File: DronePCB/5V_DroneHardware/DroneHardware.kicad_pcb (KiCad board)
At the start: 4 copper layers, 36.1 x 36 mm, 50 parts, among them J201 USB_B_Micro, J202 BATTERY, J203 SWD_CONN, J204 Conn_01x06_Male, J205 Conn_01x03_Female, J206 Conn_01x03_Female, J207 Conn_01x03_Female, J208 Conn_01x03_Female, J209 Conn_01x03_Female, J210 Conn_01x03_Female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

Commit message: Aggiunta dell'alimentazine della radio e il GND
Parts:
- added J101: +5V, Connector_PinHeader_1.00mm:PinHeader_1x01_P1.00mm_Vertical, F.Cu at (151.6, 111.4)
- added J102: GND, Connector_PinHeader_1.00mm:PinHeader_1x04_P1.00mm_Vertical, F.Cu at (135.7, 117.4)
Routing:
- net BUCK_IN: track 5.21 -> 12.9 mm
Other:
- board text added: "R_5V"
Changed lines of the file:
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@@
+    )
+  )
+  (footprint "Connector_PinHeader_1.00mm:PinHeader_1x01_P1.00mm_Vertical" (layer "F.Cu")
+    (at 151.55 111.44)
+    (descr "Through hole straight pin header, 1x01, 1.00mm pitch, single row")
+    (tags "Through hole pin header THT 1x01 1.00mm single row")
+    (property "Sheetfile" "Power.kicad_sch")
+    (property "Sheetname" "Power, Start: 100")
+    (attr through_hole)
+    (fp_text reference "J101" (at 0 -1.56) (layer "F.Fab")
+      (effects (font (size 1 1) (thickness 0.15)))
+    )
+    (fp_text value "+5V" (at 0 1.56) (layer "F.Fab")
+      (effects (font (size 1 1) (thickness 0.15)))
+    )
+    (fp_text user "${REFERENCE}" (at 0 0 90) (layer "F.Fab")
+      (effects (font (size 0.76 0.76) (thickness 0.114)))
+    )
+    (fp_line (start -0.695 0) (end -0.695 -0.685) (layer "F.SilkS") (width 0.12))
+    (fp_line (start 0.695 0.685) (end 0.695 0.56) (layer "F.SilkS") (width 0.12))
+    (fp_line (start -0.695 0.685) (end -0.695 0.56) (layer "F.SilkS") (width 0.12))
+    (fp_line (start -0.695 -0.685) (end 0 -0.685) (layer "F.SilkS") (width 0.12))
+    (fp_line (start 0.608276 0.685) (end 0.695 0.685) (layer "F.SilkS") (width 0.12))
+    (fp_line (start -0.695 0.685) (end -0.608276 0.685) (layer "F.SilkS") (width 0.12))
+    (fp_line (start -0.695 0.685) (end 0.695 0.685) (layer "F.SilkS") (width 0.12))
+    (fp_line (start 1.15 -1) (end -1.15 -1) (layer "F.CrtYd") (width 0.05))
+    (fp_line (start -1.15 1) (end 1.15 1) (layer "F.CrtYd") (width 0.05))
+    (fp_line (start 1.15 1) (end 1.15 -1) (layer "F.CrtYd") (width 0.05))
+    (fp_line (start -1.15 -1) (end -1.15 1) (layer "F.CrtYd") (width 0.05))
+    (fp_line (start -0.635 -0.1825) (end -0.3175 -0.5) (layer "F.Fab") (width 0.1))
+    (fp_line (start 0.635 0.5) (end -0.635 0.5) (layer "F.Fab") (width 0.1))
+    (fp_line (start 0.635 -0.5) (end 0.635 0.5) (layer "F.Fab") (width 0.1))
+    (fp_line (start -0.635 0.5) (end -0.635 -0.1825) (layer "F.Fab") (width 0.1))
+    (fp_line (start -0.3175 -0.5) (end 0.635 -0.5) (layer "F.Fab") (width 0.1))
+    (pad "1" thru_hole rect (at 0 0) (size 0.85 0.85) (drill 0.5) (layers *.Cu *.Mask)
+      (net 5 "BUCK_IN") (pinfunction "Pin_1") (pintype "passive"))
+    (model "${KICAD6_3DMODEL_DIR}/Connector_PinHeader_1.00mm.3dshapes/PinHeader_1x01_P1.00mm_Vertical.wrl"
+      (offset (xyz 0 0 0))
+      (scale (xyz 1 1 1))
+      (rotate (xyz 0 0 0))
     )
   )
@@
     )
   )
+  (footprint "Connector_PinHeader_1.00mm:PinHeader_1x04_P1.00mm_Vertical" (layer "F.Cu")
+    (at 135.71 117.41 90)
+    (descr "Through hole straight pin header, 1x04, 1.00mm pitch, single row")
+    (tags "Through hole pin header THT 1x04 1.00mm single row")
+    (property "Sheetfile" "Power.kicad_sch")
+    (property "Sheetname" "Power, Start: 100")
+    (attr through_hole)
+    (fp_text reference "J102" (at 0 -1.56 90) (layer "F.Fab")
+      (effects (font (size 1 1) (thickness 0.15)))
+    )
+    (fp_text value "GND" (at 0 4.56 90) (layer "F.Fab")
+      (effects (font (size 1 1) (thickness 0.15)))
+    )
+    (fp_text user "${REFERENCE}" (at 0 1.5) (layer "F.Fab")
+      (effects (font (size 0.76 0.76) (thickness 0.114)))
+    )
+    (fp_line (start 0.608276 0.685) (end 0.695 0.685) (layer "F.SilkS") (width 0.12))
+    (fp_line (start -0.695 0) (end -0.695 -0.685) (layer "F.SilkS") (width 0.12))
+    (fp_line (start -0.695 3.56) (end -0.394493 3.56) (layer "F.SilkS") (width 0.12))
+    (fp_line (start -0.695 0.685) (end -0.608276 0.685) (layer "F.SilkS") (width 0.12))
+    (fp_line (start -0.695 -0.685) (end 0 -0.685) (layer "F.SilkS") (width 0.12))
+    (fp_line (start 0.394493 3.56) (end 0.695 3.56) (layer "F.SilkS") (width 0.12))
+    (fp_line (start 0.695 0.685) (end 0.695 3.56) (layer "F.SilkS") (width 0.12))
+    (fp_line (start -0.695 0.685) (end -0.695 3.56) (layer "F.SilkS") (width 0.12))
+    (fp_line (start -1.15 4) (end 1.15 4) (layer "F.CrtYd") (width 0.05))
+    (fp_line (start 1.15 4) (end 1.15 -1) (layer "F.CrtYd") (width 0.05))
+    (fp_line (start -1.15 -1) (end -1.15 4) (layer "F.CrtYd") (width 0.05))
+    (fp_line (start 1.15 -1) (end -1.15 -1) (layer "F.CrtYd") (width 0.05))
+    (fp_line (start -0.635 -0.1825) (end -0.3175 -0.5) (layer "F.Fab") (width 0.1))
+    (fp_line (start -0.3175 -0.5) (end 0.635 -0.5) (layer "F.Fab") (width 0.1))
+    (fp_line (start 0.635 -0.5) (end 0.635 3.5) (layer "F.Fab") (width 0.1))
+    (fp_line (start 0.635 3.5) (end -0.635 3.5) (layer "F.Fab") (width 0.1))
+    (fp_line (start -0.635 3.5) (end -0.635 -0.1825) (layer "F.Fab") (width 0.1))
+    (pad "1" thru_hole rect (at 0 0 90) (size 0.85 0.85) (drill 0.5) (layers *.Cu *.Mask)
+      (net 2 "GND") (pinfunction "Pin_1") (pintype "passive"))
+    (pad "2" thru_hole oval (at 0 1 90) (size 0.85 0.85) (drill 0.5) (layers *.Cu *.Mask)
+      (net 2 "GND") (pinfunction "Pin_2") (pintype "passive"))
+    (pad "3" thru_hole oval (at 0 2 90) (size 0.85 0.85) (drill 0.5) (layers *.Cu *.Mask)
+      (net 2 "GND") (pinfunction "Pin_3") (pintype "passive"))
+    (pad "4" thru_hole oval (at 0 3 90) (size 0.85 0.85) (drill 0.5) (layers *.Cu *.Mask)
+      (net 2 "GND") (pinfunction "Pin_4") (pintype "passive"))
+    (model "${KICAD6_3DMODEL_DIR}/Connector_PinHeader_1.00mm.3dshapes/PinHeader_1x04_P1.00mm_Vertical.wrl"
+      (offset (xyz 0 0 0))
+      (scale (xyz 1 1 1))
+      (rotate (xyz 0 0 0))
+    )
+  )
   (footprint "Resistor_SMD:R_0603_1608Metric" (layer "F.Cu")
     (at 160.07 110.84 -90)
@@
     (at 156.23 106.85 180)
     (attr board_only exclude_from_pos_files exclude_from_bom)
-    (fp_text reference "G***" (at 0 0) (layer "B.Fab")
+    (fp_text reference "G***" (at 0 0) (layer "F.Fab")
       (effects (font (size 1.524 1.524) (thickness 0.3)) (justify mirror))
     )
-    (fp_text value "LOGO" (at 0.75 0) (layer "B.Fab") hide
+    (fp_text value "LOGO" (at 0.75 0) (layer "F.Fab") hide
       (effects (font (size 1.524 1.524) (thickness 0.3)) (justify mirror))
     )
@@
       ) (layer "B.SilkS") (width 0) (fill solid))
   )
+  (gr_line (start 134.79 118.8) (end 141.37 118.79) (layer "F.SilkS") (width 0.15))
   (gr_arc (start 130.548478 119.07) (mid 128.710272 118.299778) (end 127.940001 116.461592) (layer "Edge.Cuts") (width 0.1))
   (gr_arc (start 161.441522 83.078478) (mid 163.286553 83.839188) (end 164.061432 85.678313) (layer "Edge.Cuts") (width 0.1))
@@
     (effects (font (size 0.5 0.5) (thickness 0.1)))
   )
+  (gr_text "R_5V\n" (at 151.42 112.85) (layer "F.SilkS")
+    (effects (font (size 0.5 0.5) (thickness 0.1)))
+  )
   (gr_text "GND\n" (at 150.87 117.85) (layer "F.SilkS")
     (effects (font (size 0.5 0.5) (thickness 0.1)))
@@
   )
   (gr_text "4" (at 132.28 103.54) (layer "F.SilkS")
+    (effects (font (size 0.5 0.5) (thickness 0.1)))
+  )
+  (gr_text "GND\n" (at 140.74 118.25) (layer "F.SilkS")
     (effects (font (size 0.5 0.5) (thickness 0.1)))
   )
@@
   (segment (start 137.16 97.14) (end 137.85 97.83) (width 0.3) (layer "F.Cu") (net 4))
   (segment (start 158.275 110.48) (end 158.275 112.5525) (width 0.6) (layer "F.Cu") (net 5))
+  (segment (start 157.66 107.72) (end 155.27 107.72) (width 0.6) (layer "F.Cu") (net 5))
   (segment (start 158.275 112.5525) (end 158.3625 112.64) (width 0.6) (layer "F.Cu") (net 5))
+  (segment (start 155.27 107.72) (end 151.55 111.44) (width 0.6) (layer "F.Cu") (net 5))
   (segment (start 157.66 109.865) (end 158.275 110.48) (width 0.6) (layer "F.Cu") (net 5))
   (segment (start 157.66 107.72) (end 157.66 109.865) (width 0.6) (layer "F.Cu") (net 5))

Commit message: BOM e pos file
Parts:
- C102: footprint Capacitor_SMD:C_0201_0603Metric -> Capacitor_Tantalum_SMD:CP_EIA-1608-08_AVX-J
- moved R101 0.63 mm to (160.0, 111.5)
- moved D102 0.52 mm to (162.4, 112.1)
- moved C102 0.50 mm to (162.4, 110.0)
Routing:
- net GND: track 41.8 -> 43.7 mm, vias 31 -> 30
- net BUCK_VOUT_3V3: track 27.0 -> 28.2 mm

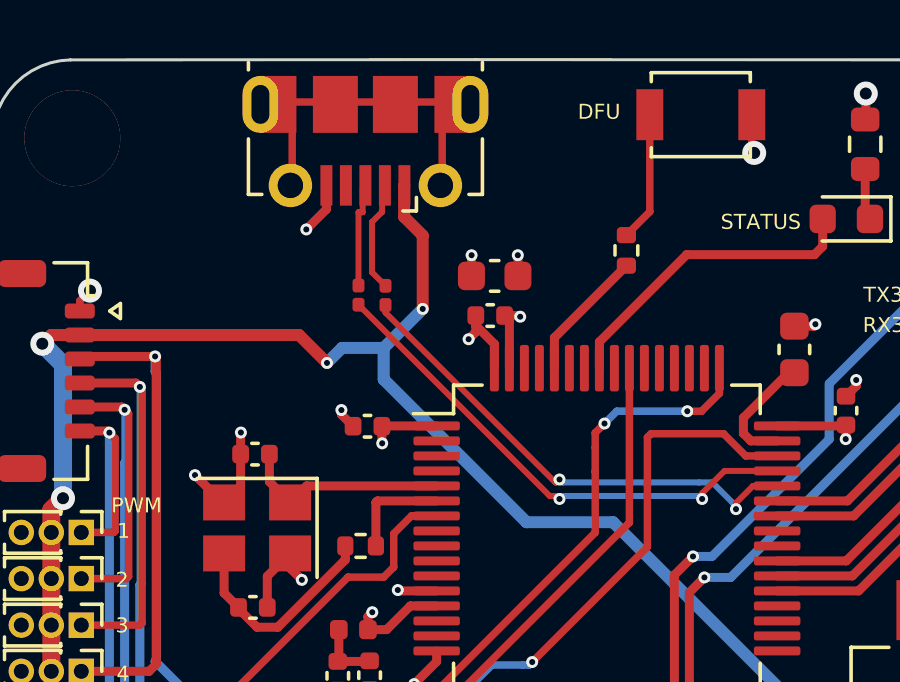
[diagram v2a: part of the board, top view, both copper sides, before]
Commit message: Modifica delle componenti 0201 in componenti 0402
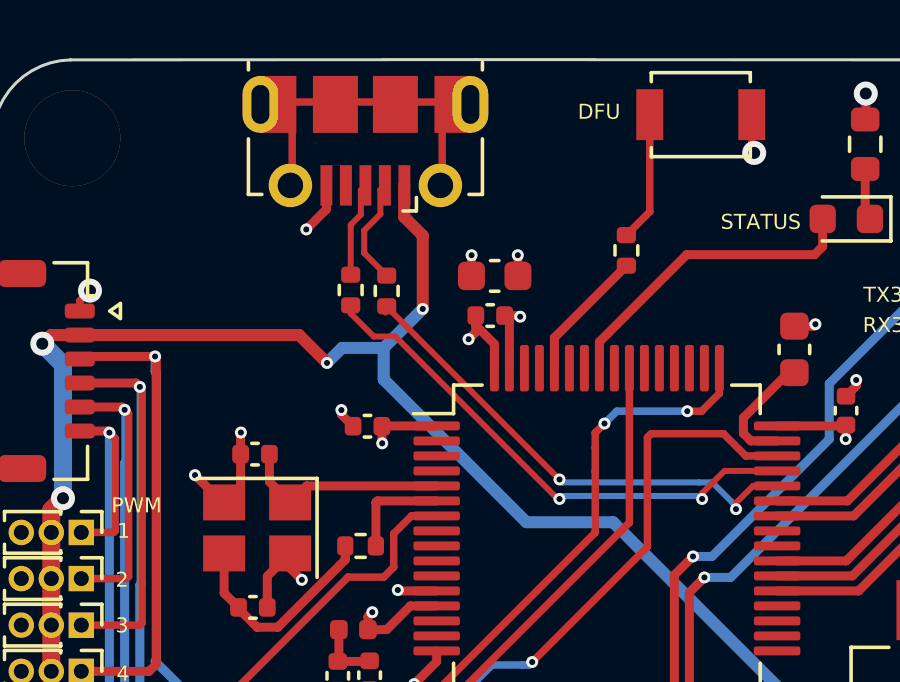
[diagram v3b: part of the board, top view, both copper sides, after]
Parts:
- R201, R202: footprint Resistor_SMD:R_0201_0603Metric -> Resistor_SMD:R_0402_1005Metric
- moved R201 0.31 mm to (139.9, 90.8)
- moved R202 0.16 mm to (141.1, 90.8), turned to -90 degrees
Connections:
- R202 pad 1: USB_D- -> USB_CONN_D-
- R202 pad 2: USB_CONN_D- -> USB_D-

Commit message: Scheda Vespin 1.0 fatta spampare
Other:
- board text added: "+"
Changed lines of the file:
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@@
       ) (layer "B.SilkS") (width 0) (fill solid))
   )
+  (gr_circle (center 147.382982 110.95) (end 147.622982 111.03) (layer "F.SilkS") (width 0.15) (fill none))
+  (gr_circle (center 155.962982 107.03) (end 156.202982 107.11) (layer "F.SilkS") (width 0.15) (fill none))
   (gr_line (start 134.79 118.8) (end 141.37 118.79) (layer "F.SilkS") (width 0.15))
+  (gr_circle (center 138.462982 96.39) (end 138.702982 96.47) (layer "F.SilkS") (width 0.15) (fill none))
+  (gr_circle (center 141.977018 94.17) (end 142.217018 94.25) (layer "F.SilkS") (width 0.15) (fill none))
   (gr_arc (start 130.548478 119.07) (mid 128.710272 118.299778) (end 127.940001 116.461592) (layer "Edge.Cuts") (width 0.1))
   (gr_arc (start 161.441522 83.078478) (mid 163.286553 83.839188) (end 164.061432 85.678313) (layer "Edge.Cuts") (width 0.1))
@@
     (effects (font (size 0.5 0.5) (thickness 0.1)) (justify left mirror))
   )
+  (gr_text "+" (at 154.91 87.55) (layer "F.SilkS")
+    (effects (font (size 0.5 0.5) (thickness 0.1)))
+  )
   (gr_text "DFU" (at 148.15 84.81) (layer "F.SilkS")
     (effects (font (size 0.5 0.5) (thickness 0.1)))
@@
   )
   (gr_text "CK6" (at 160.91 95.44) (layer "F.SilkS")
+    (effects (font (size 0.5 0.5) (thickness 0.1)))
+  )
+  (gr_text "+" (at 163.72 113.09) (layer "F.SilkS")
     (effects (font (size 0.5 0.5) (thickness 0.1)))
   )
@@
   )
   (gr_text "GND\n" (at 150.87 117.85) (layer "F.SilkS")
+    (effects (font (size 0.5 0.5) (thickness 0.1)))
+  )
+  (gr_text "+" (at 155.55 118.32) (layer "F.SilkS")
     (effects (font (size 0.5 0.5) (thickness 0.1)))
   )
@@
     (effects (font (size 0.5 0.5) (thickness 0.1)))
   )
+  (gr_text "+" (at 163.54 108.77) (layer "F.SilkS")
+    (effects (font (size 0.5 0.5) (thickness 0.1)))
+  )

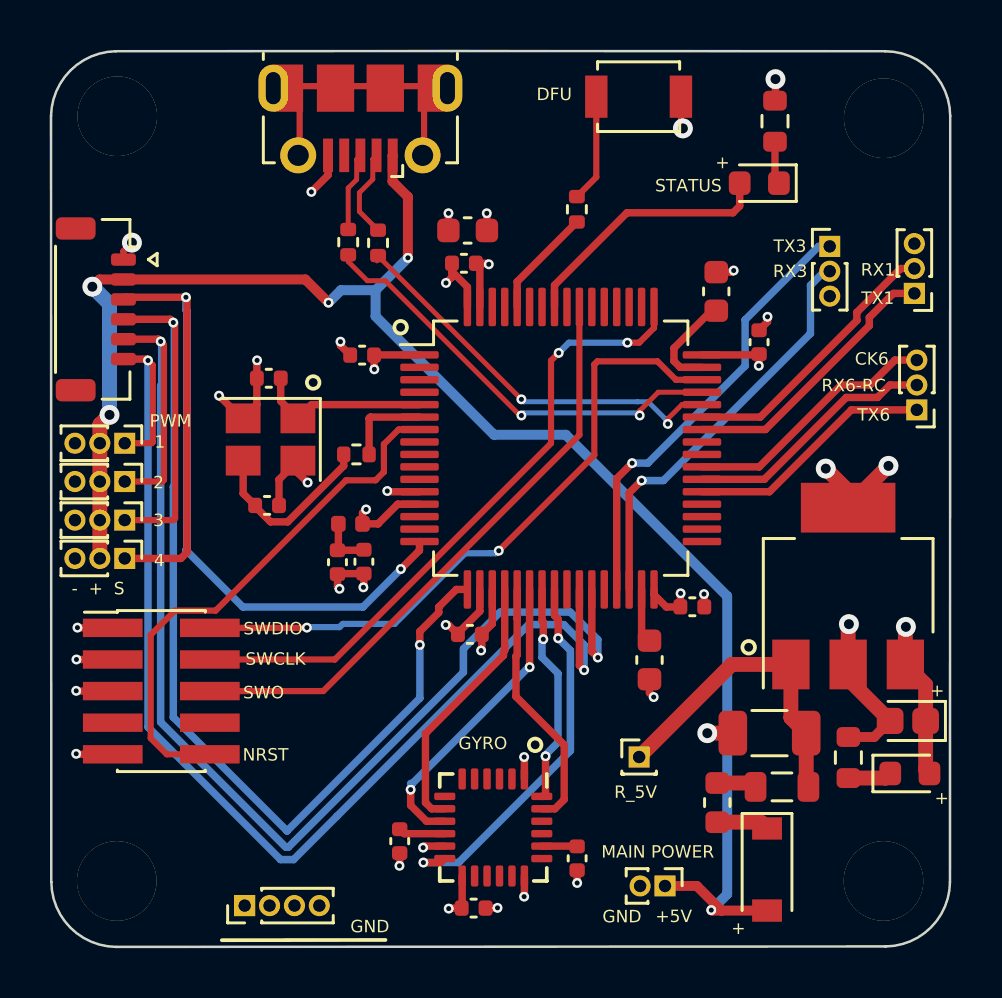
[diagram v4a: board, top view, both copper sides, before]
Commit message: Passaggio delle Vie da 0.2 a 0.4 mm
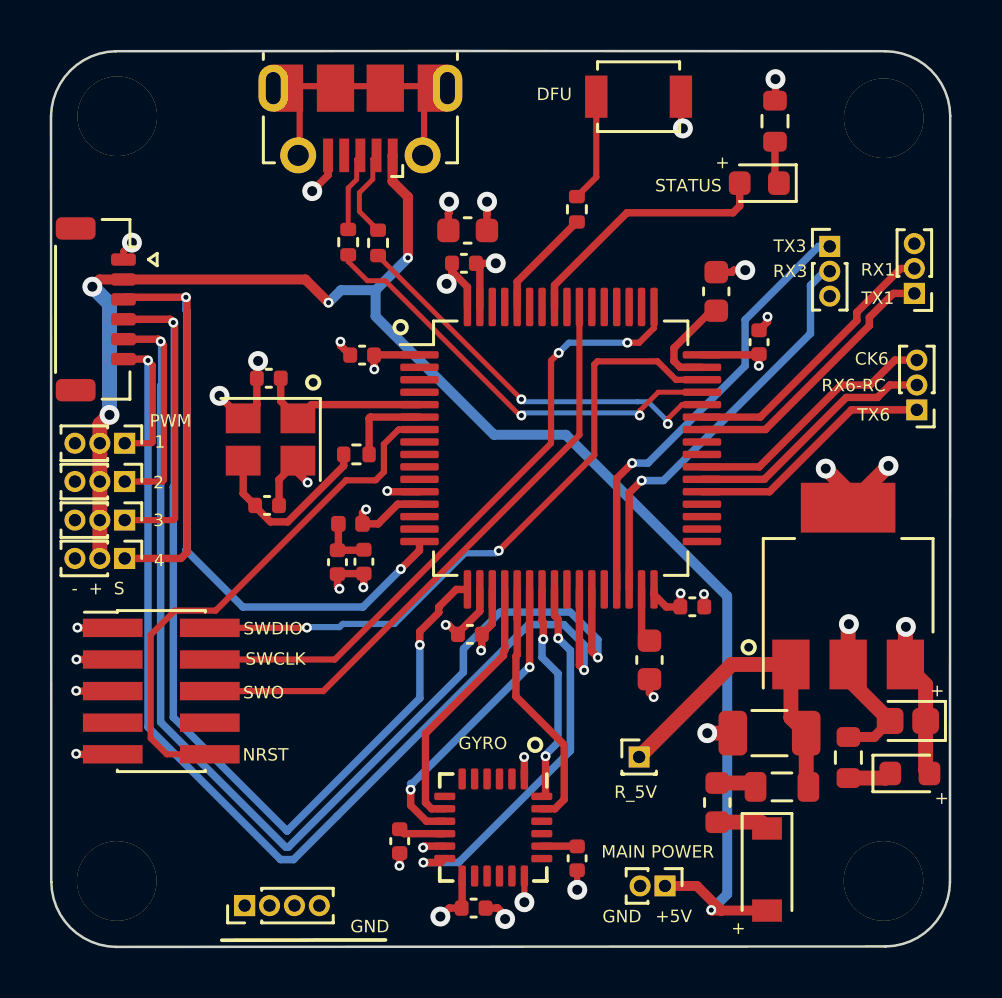
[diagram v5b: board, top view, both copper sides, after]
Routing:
- net GND: track 43.7 -> 46.0 mm
- net BUCK_VOUT_3V3: track 28.2 -> 29.1 mm

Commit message: Aggiornamento delle vie da 0.2 a 0.4 mm, mancano le vie di pwm, le vie relative a MPU6000 e relative e USB
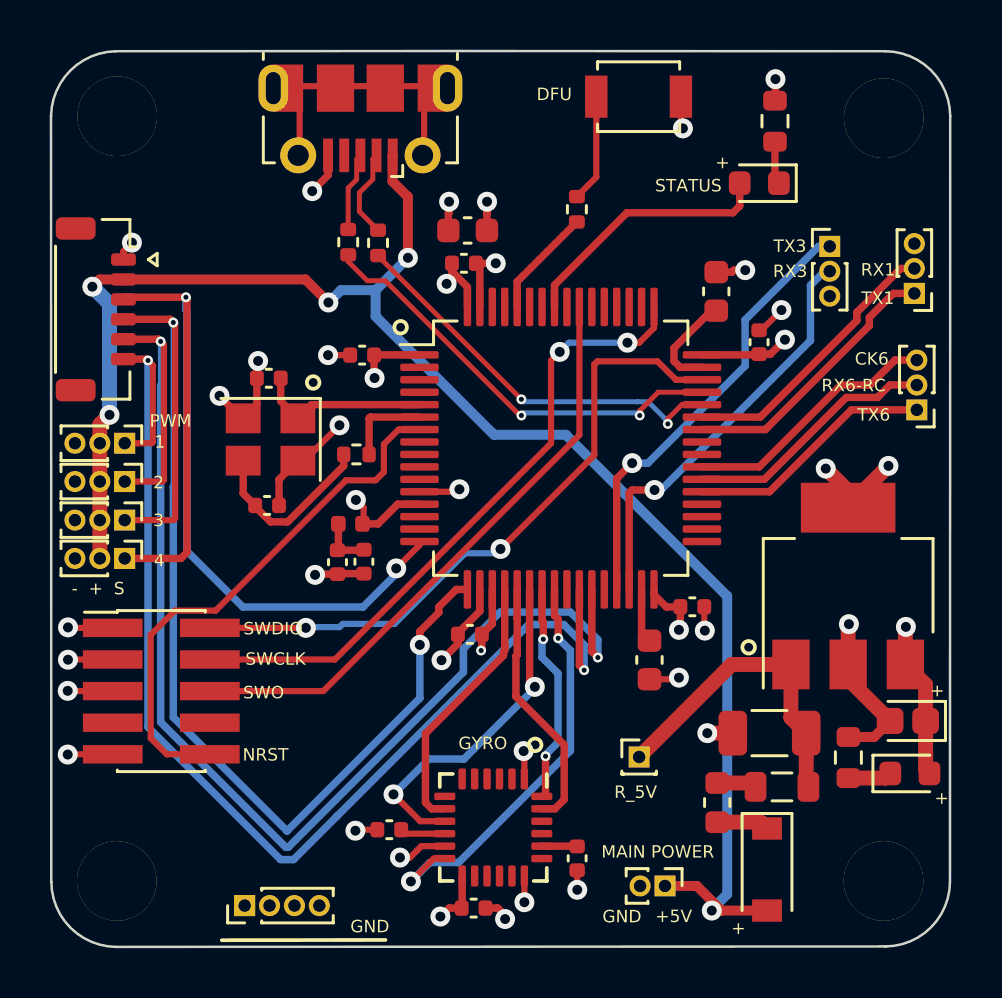
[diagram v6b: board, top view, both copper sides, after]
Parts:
- moved C316 0.62 mm to (141.5, 114.4), turned to 180 degrees
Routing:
- net GND: track 46.0 -> 52.7 mm, vias 30 -> 29
- net BUCK_VOUT_3V3: track 29.1 -> 31.5 mm
- net GYRO_MISO_PIN: track 12.4 -> 14.0 mm
- net GYRO_INT_EXTI: track 15.4 -> 17.1 mm

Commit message: In stampa 22 agosto 2022
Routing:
- net PWM4: track 37.2 -> 43.6 mm
- net PWM3: track 47.3 -> 52.3 mm
- net PWM2: track 52.2 -> 56.3 mm
- net PWM1: track 48.6 -> 51.4 mm
- net USB_D+: track 17.6 -> 18.8 mm
- net GYRO_INT_EXTI: track 17.1 -> 17.8 mm
